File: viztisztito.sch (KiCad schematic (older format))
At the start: 5 parts, among them P2 BOARD_CONN, P3 SSR&PWR, P5 CONN_01X04, P6 CONN_01X02, P9 CONN_01X10

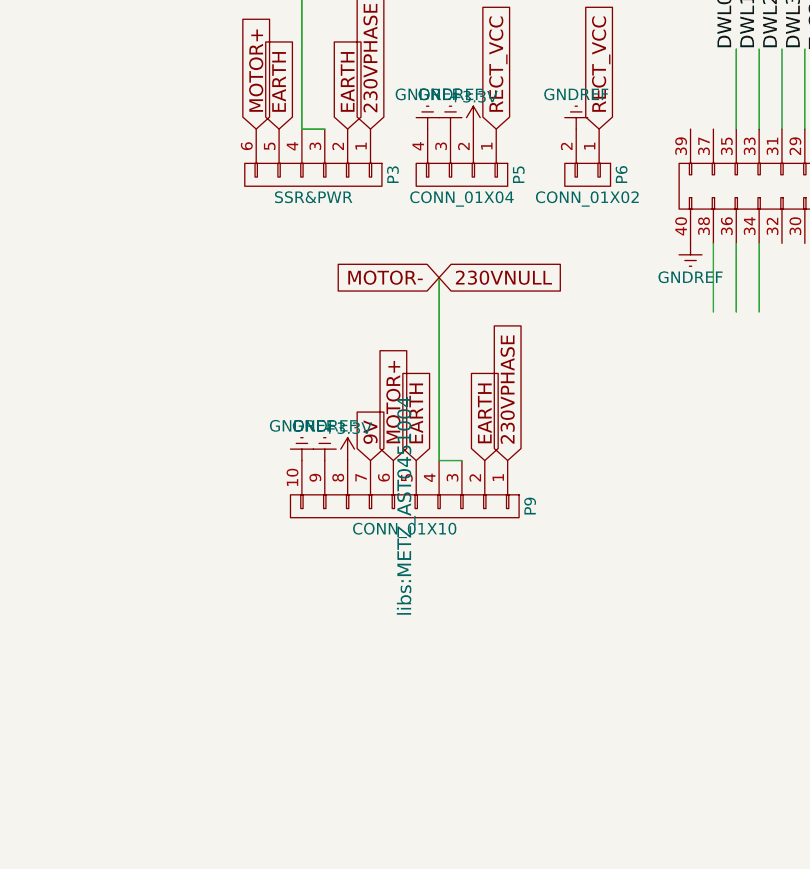
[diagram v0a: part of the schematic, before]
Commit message: - snubber circuit added - diodes selected
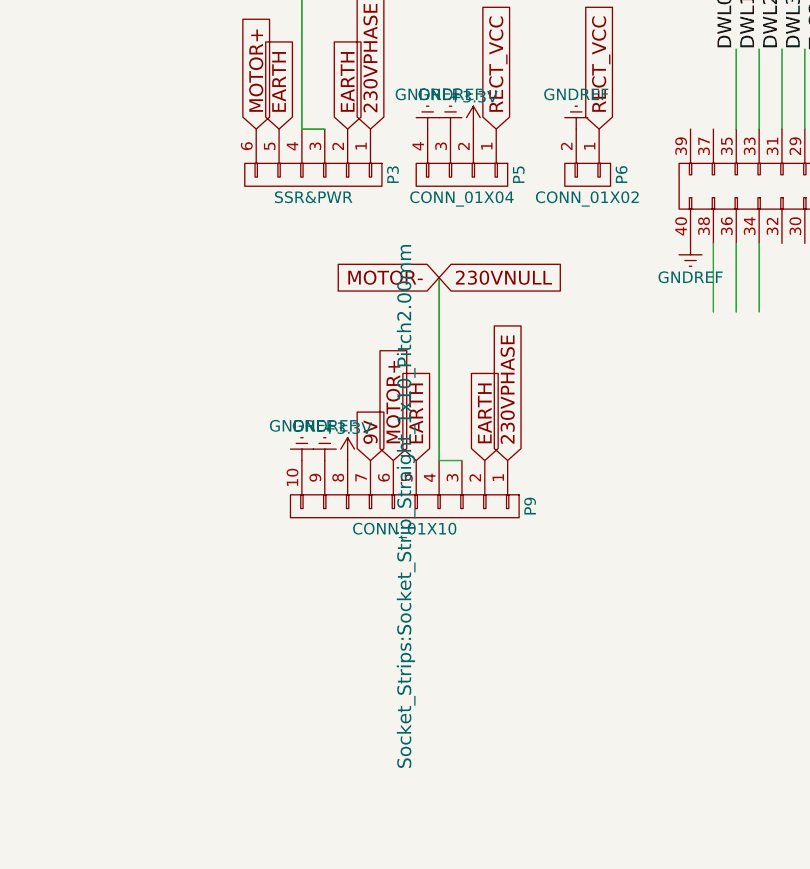
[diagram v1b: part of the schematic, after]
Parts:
- P2: footprint Socket_Strips:Socket_Strip_Straight_2x20 -> Socket_Strips:Socket_Strip_Straight_2x20_Pitch2.54mm
- P3: footprint libs:METZ_AST1350604 -> Connectors:PINHEAD1-6
- P5: footprint libs:METZ_AST1350404 -> Connectors:Grove_1x04
- P6: footprint Pin_Headers:Pin_Header_Straight_1x02 -> Pin_Headers:Pin_Header_Angled_1x02_Pitch2.54mm
- P9: footprint libs:METZ_AST0451004 -> Socket_Strips:Socket_Strip_Straight_1x10_Pitch2.00mm
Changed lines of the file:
@@
 F 0 "P3" H 6150 5150 50  0000 C CNN
 F 1 "SSR&PWR" V 6250 4800 50  0000 C CNN
-F 2 "libs:METZ_AST1350604" H 6150 4800 60  0001 C CNN
+F 2 "Connectors:PINHEAD1-6" H 6150 4800 60  0001 C CNN
 F 3 "" H 6150 4800 60  0000 C CNN
 	1    6150 4800
@@
 F 0 "P2" H 8750 5900 50  0000 C CNN
 F 1 "BOARD_CONN" V 8750 4850 50  0000 C CNN
-F 2 "Socket_Strips:Socket_Strip_Straight_2x20" H 8750 3900 60  0001 C CNN
+F 2 "Socket_Strips:Socket_Strip_Straight_2x20_Pitch2.54mm" H 8750 3900 60  0001 C CNN
 F 3 "" H 8750 3900 60  0000 C CNN
 	1    8750 4850
@@
 F 0 "P5" H 6800 5050 50  0000 C CNN
 F 1 "CONN_01X04" V 6900 4800 50  0000 C CNN
-F 2 "libs:METZ_AST1350404" H 6800 4800 60  0001 C CNN
+F 2 "Connectors:Grove_1x04" H 6800 4800 60  0001 C CNN
 F 3 "" H 6800 4800 60  0000 C CNN
 	1    6800 4800
@@
 F 0 "P6" H 7350 4950 50  0000 C CNN
 F 1 "CONN_01X02" V 7450 4800 50  0000 C CNN
-F 2 "Pin_Headers:Pin_Header_Straight_1x02" H 7350 4800 60  0001 C CNN
+F 2 "Pin_Headers:Pin_Header_Angled_1x02_Pitch2.54mm" H 7350 4800 60  0001 C CNN
 F 3 "" H 7350 4800 60  0000 C CNN
 	1    7350 4800
@@
 F 0 "P9" H 6550 6800 50  0000 C CNN
 F 1 "CONN_01X10" V 6650 6250 50  0000 C CNN
-F 2 "libs:METZ_AST0451004" H 6550 6250 60  0000 C CNN
+F 2 "Socket_Strips:Socket_Strip_Straight_1x10_Pitch2.00mm" H 6550 6250 60  0000 C CNN
 F 3 "" H 6550 6250 60  0000 C CNN
 	1    6550 6250

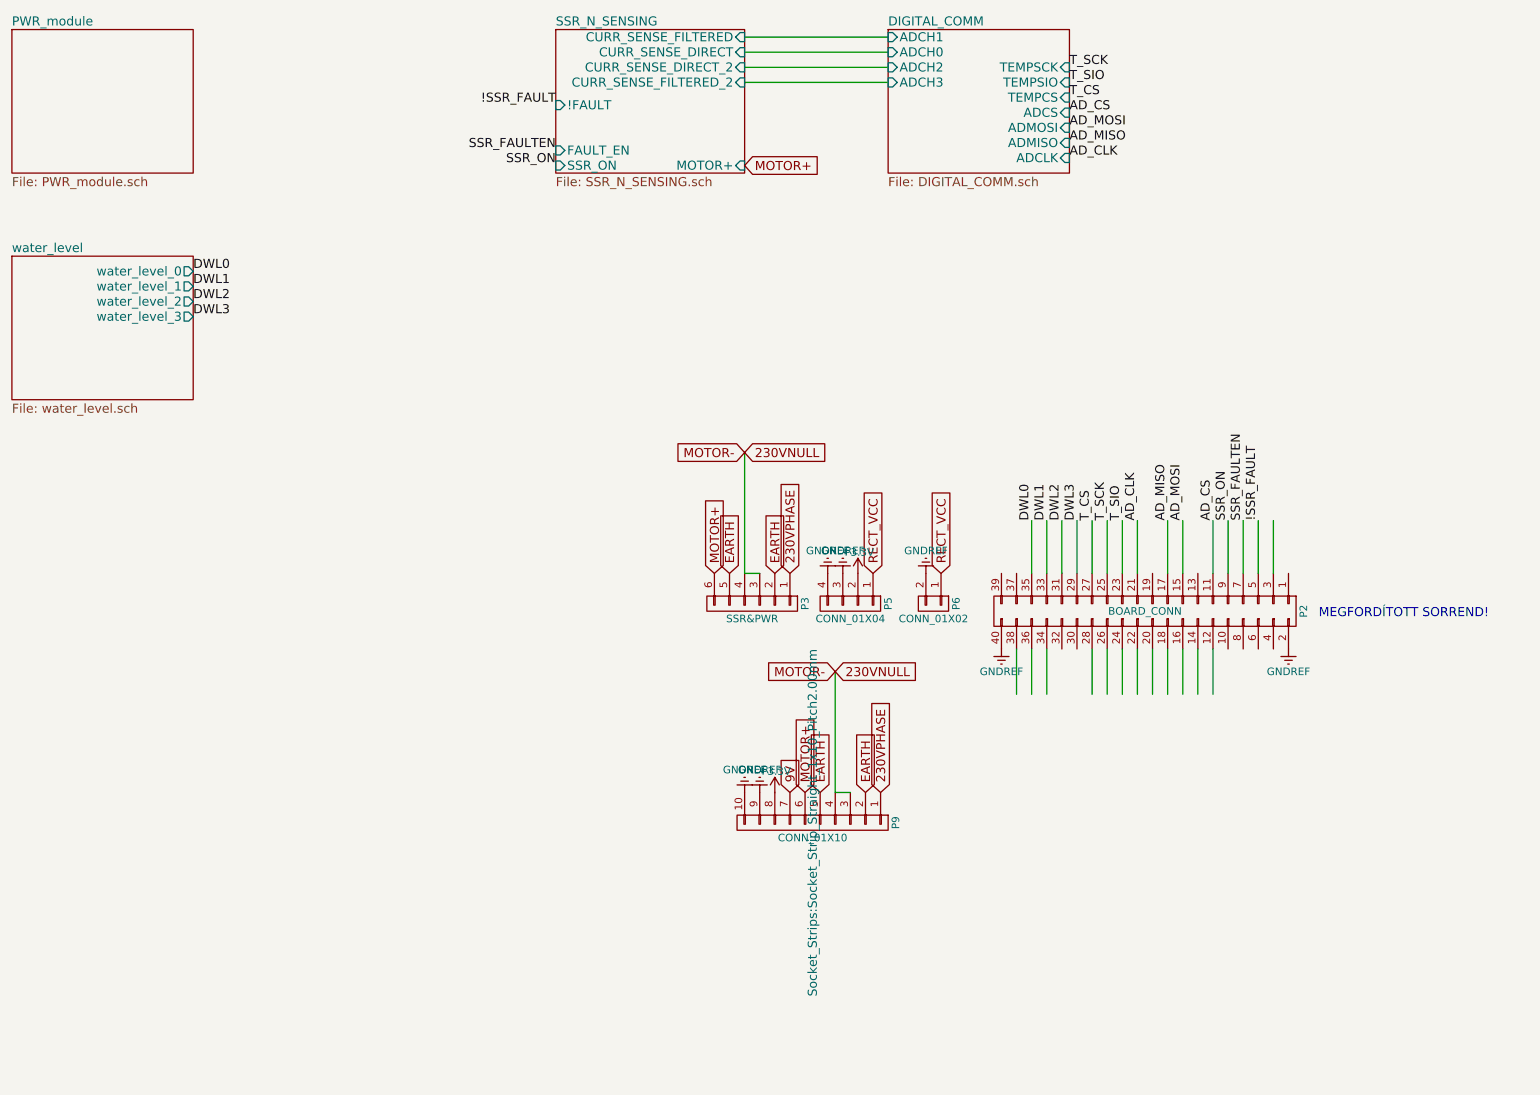
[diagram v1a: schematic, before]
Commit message: all components verified, pcb design required
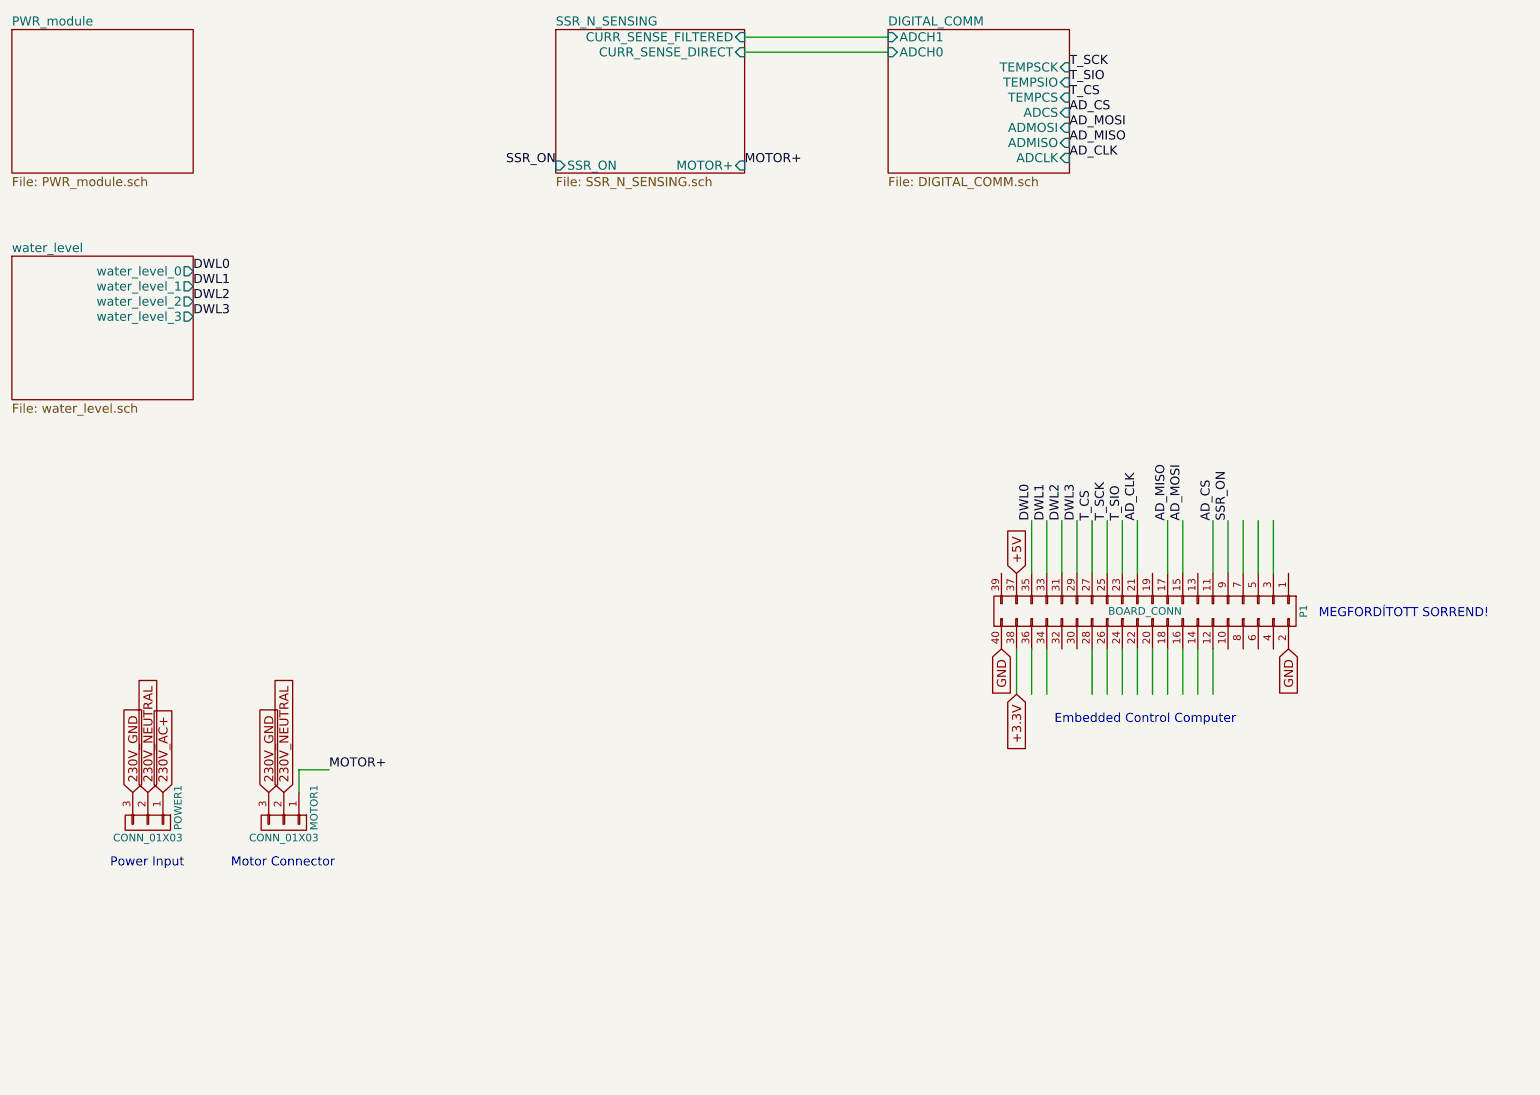
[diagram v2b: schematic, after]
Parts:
- removed P3: SSR&PWR, Connectors:PINHEAD1-6, symbol CONN_01X06
- removed P5: CONN_01X04, Connectors:Grove_1x04, symbol CONN_01X04
- removed P6: CONN_01X02, Pin_Headers:Pin_Header_Angled_1x02_Pitch2.54mm, symbol CONN_01X02
- removed P9: CONN_01X10, Socket_Strips:Socket_Strip_Straight_1x10_Pitch2.00mm, symbol CONN_01X10
- added MOTOR1, POWER1: CONN_01X03, Connectors_Terminal_Blocks:TerminalBlock_WAGO-236_2Stift_RM5mm_3pol, symbol CONN_01X03
- renumbered P2 to P1
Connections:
- net labels added: +5V, 230V_AC+, 230V_GND, 230V_NEUTRAL, GND
- net labels removed: !SSR_FAULT, 230VNULL, 230VPHASE, 9V, EARTH, GNDREF, MOTOR-, RECT_VCC, SSR_FAULTEN
- wire segments 35 -> 31
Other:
- note added: "Embedded Control Computer"
- note added: "Motor Connector"
- note added: "Power Input"

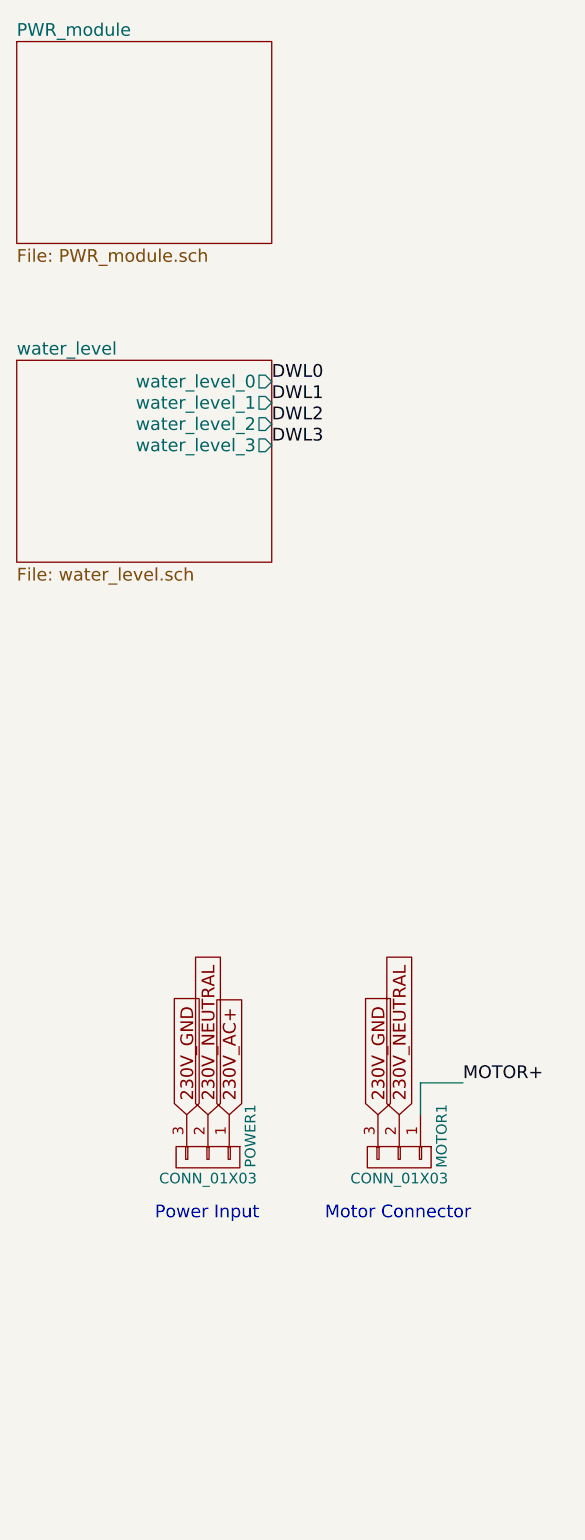
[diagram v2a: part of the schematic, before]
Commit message: this version has the parts organized; before routing
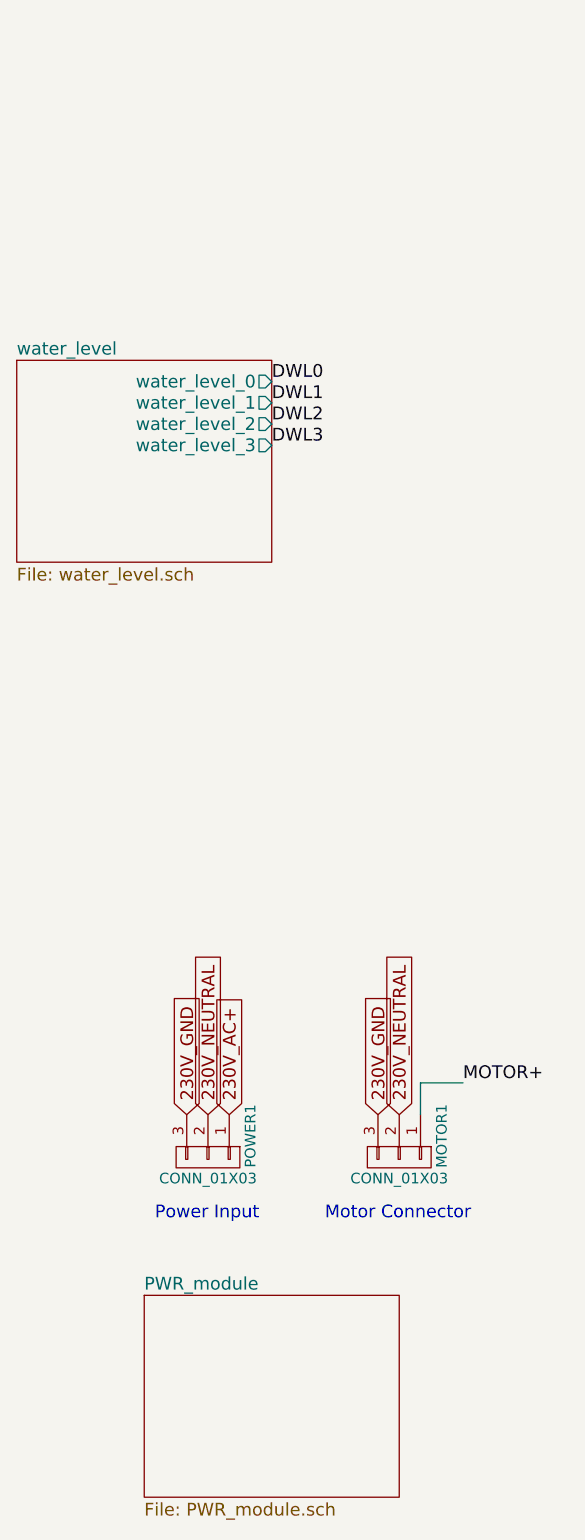
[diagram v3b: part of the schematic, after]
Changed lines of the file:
@@
 $EndDescr
 $Sheet
-S 1250 1000 1200 950
+S 1850 6900 1200 950
 U 5614D811
 F0 "PWR_module" 60

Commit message: updated links
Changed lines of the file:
@@
 F 1 "BOARD_CONN" V 8750 4850 50  0000 C CNN
 F 2 "Socket_Strips:Socket_Strip_Straight_2x20_Pitch2.54mm" H 8750 3900 60  0001 C CNN
-F 3 "" H 8750 3900 60  0000 C CNN
+F 3 "http://hu.farnell.com/samtec/tsw-120-07-t-d/connector-header-40pos-2row-2/dp/2667451" H 8750 3900 60  0000 C CNN
 	1    8750 4850
 	0    1    1    0

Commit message: stash commit before the revision of the parts
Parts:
- P1: idc connector (none) -> http://hu.farnell.com/3m/d89140-0031hk/connector-rcpt-40pos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; ribbon cable (none) -> http://hu.farnell.com/pro-power/r2651dtsy40sc85/ribbon-cabl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
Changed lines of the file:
@@
 F 1 "BOARD_CONN" V 8750 4850 50  0000 C CNN
 F 2 "Socket_Strips:Socket_Strip_Straight_2x20_Pitch2.54mm" H 8750 3900 60  0001 C CNN
-F 3 "http://hu.farnell.com/samtec/tsw-120-07-t-d/connector-header-40pos-2row-2/dp/2667451" H 8750 3900 60  0000 C CNN
+F 3 "http://hu.farnell.com/wurth-elektronik/61304021021/header-2-54mm-pin-tht-r-a-40way/dp/2356207" H 8750 3900 60  0000 C CNN
+F 4 "http://hu.farnell.com/3m/d89140-0031hk/connector-rcpt-40pos-2row-2-54mm/dp/2672516" H 8750 4850 60  0001 C CNN "idc connector"
+F 5 "http://hu.farnell.com/pro-power/r2651dtsy40sc85/ribbon-cable-40-core-28awg-per/dp/2628367" H 8750 4850 60  0001 C CNN "ribbon cable"
 	1    8750 4850
 	0    1    1    0
@@
 F 1 "CONN_01X03" V 2250 6250 50  0000 C CNN
 F 2 "Connectors_Terminal_Blocks:TerminalBlock_WAGO-236_2Stift_RM5mm_3pol" H 2150 6250 50  0001 C CNN
-F 3 "http://hu.farnell.com/wago/2092-1173/terminal-block-wire-to-brd-3pos/dp/2352396" H 2150 6250 50  0001 C CNN
+F 3 "http://hu.farnell.com/wago/2604-1103/tb-wire-to-brd-3pos-12awg/dp/2749666" H 2150 6250 50  0001 C CNN
 	1    2150 6250
 	0    1    1    0
@@
 F 1 "CONN_01X03" V 3150 6250 50  0000 C CNN
 F 2 "Connectors_Terminal_Blocks:TerminalBlock_WAGO-236_2Stift_RM5mm_3pol" H 3050 6250 50  0001 C CNN
-F 3 "http://hu.farnell.com/wago/2092-1173/terminal-block-wire-to-brd-3pos/dp/2352396" H 3050 6250 50  0001 C CNN
+F 3 "http://hu.farnell.com/wago/2604-1103/tb-wire-to-brd-3pos-12awg/dp/2749666" H 3050 6250 50  0001 C CNN
 	1    3050 6250
 	0    1    1    0

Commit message: parts corrected after review; dc/dc converter has to be ordered
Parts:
- MOTOR1, POWER1: footprint Connectors_Terminal_Blocks:TerminalBlock_WAGO-236_2Stift_RM5mm_3pol -> Connectors_Terminal_Blocks:TerminalBlock_WAGO-804_RM5mm_3pol
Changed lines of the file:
@@
 F 0 "POWER1" H 2050 6450 50  0000 C CNN
 F 1 "CONN_01X03" V 2250 6250 50  0000 C CNN
-F 2 "Connectors_Terminal_Blocks:TerminalBlock_WAGO-236_2Stift_RM5mm_3pol" H 2150 6250 50  0001 C CNN
+F 2 "Connectors_Terminal_Blocks:TerminalBlock_WAGO-804_RM5mm_3pol" H 2150 6250 50  0001 C CNN
 F 3 "http://hu.farnell.com/wago/2604-1103/tb-wire-to-brd-3pos-12awg/dp/2749666" H 2150 6250 50  0001 C CNN
 	1    2150 6250
@@
 F 0 "MOTOR1" H 2950 6450 50  0000 C CNN
 F 1 "CONN_01X03" V 3150 6250 50  0000 C CNN
-F 2 "Connectors_Terminal_Blocks:TerminalBlock_WAGO-236_2Stift_RM5mm_3pol" H 3050 6250 50  0001 C CNN
+F 2 "Connectors_Terminal_Blocks:TerminalBlock_WAGO-804_RM5mm_3pol" H 3050 6250 50  0001 C CNN
 F 3 "http://hu.farnell.com/wago/2604-1103/tb-wire-to-brd-3pos-12awg/dp/2749666" H 3050 6250 50  0001 C CNN
 	1    3050 6250

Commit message: before wiring
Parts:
- P1: footprint Socket_Strips:Socket_Strip_Straight_2x20_Pitch2.54mm -> water:olinuxino_im233_ver2
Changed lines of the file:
@@
 F 0 "P1" H 8750 5900 50  0000 C CNN
 F 1 "BOARD_CONN" V 8750 4850 50  0000 C CNN
-F 2 "Socket_Strips:Socket_Strip_Straight_2x20_Pitch2.54mm" H 8750 3900 60  0001 C CNN
+F 2 "water:olinuxino_im233_ver2" H 8750 3900 60  0001 C CNN
 F 3 "http://hu.farnell.com/wurth-elektronik/61304021021/header-2-54mm-pin-tht-r-a-40way/dp/2356207" H 8750 3900 60  0000 C CNN
 F 4 "http://hu.farnell.com/3m/d89140-0031hk/connector-rcpt-40pos-2row-2-54mm/dp/2672516" H 8750 4850 60  0001 C CNN "idc connector"

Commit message: shields corrected; wago connectors connected
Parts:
- MOTOR1, POWER1: footprint Connectors_Terminal_Blocks:TerminalBlock_WAGO-804_RM5mm_3pol -> water:3x1_TerminalBlock_WAGO-804_RM5mm_3pol
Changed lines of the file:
@@
 F 0 "POWER1" H 2050 6450 50  0000 C CNN
 F 1 "CONN_01X03" V 2250 6250 50  0000 C CNN
-F 2 "Connectors_Terminal_Blocks:TerminalBlock_WAGO-804_RM5mm_3pol" H 2150 6250 50  0001 C CNN
+F 2 "water:3x1_TerminalBlock_WAGO-804_RM5mm_3pol" H 2150 6250 50  0001 C CNN
 F 3 "http://hu.farnell.com/wago/2604-1103/tb-wire-to-brd-3pos-12awg/dp/2749666" H 2150 6250 50  0001 C CNN
 	1    2150 6250
@@
 F 0 "MOTOR1" H 2950 6450 50  0000 C CNN
 F 1 "CONN_01X03" V 3150 6250 50  0000 C CNN
-F 2 "Connectors_Terminal_Blocks:TerminalBlock_WAGO-804_RM5mm_3pol" H 3050 6250 50  0001 C CNN
+F 2 "water:3x1_TerminalBlock_WAGO-804_RM5mm_3pol" H 3050 6250 50  0001 C CNN
 F 3 "http://hu.farnell.com/wago/2604-1103/tb-wire-to-brd-3pos-12awg/dp/2749666" H 3050 6250 50  0001 C CNN
 	1    3050 6250
